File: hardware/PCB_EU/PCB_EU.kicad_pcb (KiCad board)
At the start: 4 copper layers, 100 x 100 mm, 200 parts, among them J101 24 V IN, J201 UART 3V3, J301 MEM2061 SPI, J401 SHT4x XH2.54-4P-90, J403 FLOAT / GND, J411 FAN1 2510-4P, J421 FAN2 2510-4P, J501 LED1 + / GND, J601 LED2 + / GND, J602 BAR2 + / GND, J701 PTC + / RETURN, J702 PUMP + / RETURN, Q102 IRF1010ESPBF, Q411 FAN1 AO3422, Q421 FAN2 AO3422, Q501 TK22E10N1, Q601 TK22E10N1, Q701 BC847B-DIO, Q702 BC857B, Q703 IRF1010ESPBF, Q704 AO3422, SW201 RESET, SW202 BOOT, U101 L7987 3A, U102 INA226, U201 AP63203WU-7, U202 ESP32-WROOM-32E-N4, U301 MCP7940N-I/SN, U401 USBLC6-2SC6, U402 USBLC6-2SC6, U501 LM3429MH/NOPB, U601 LM3429MH/NOPB, U802 LM2903D-ST, Y301 32.768k CL7p

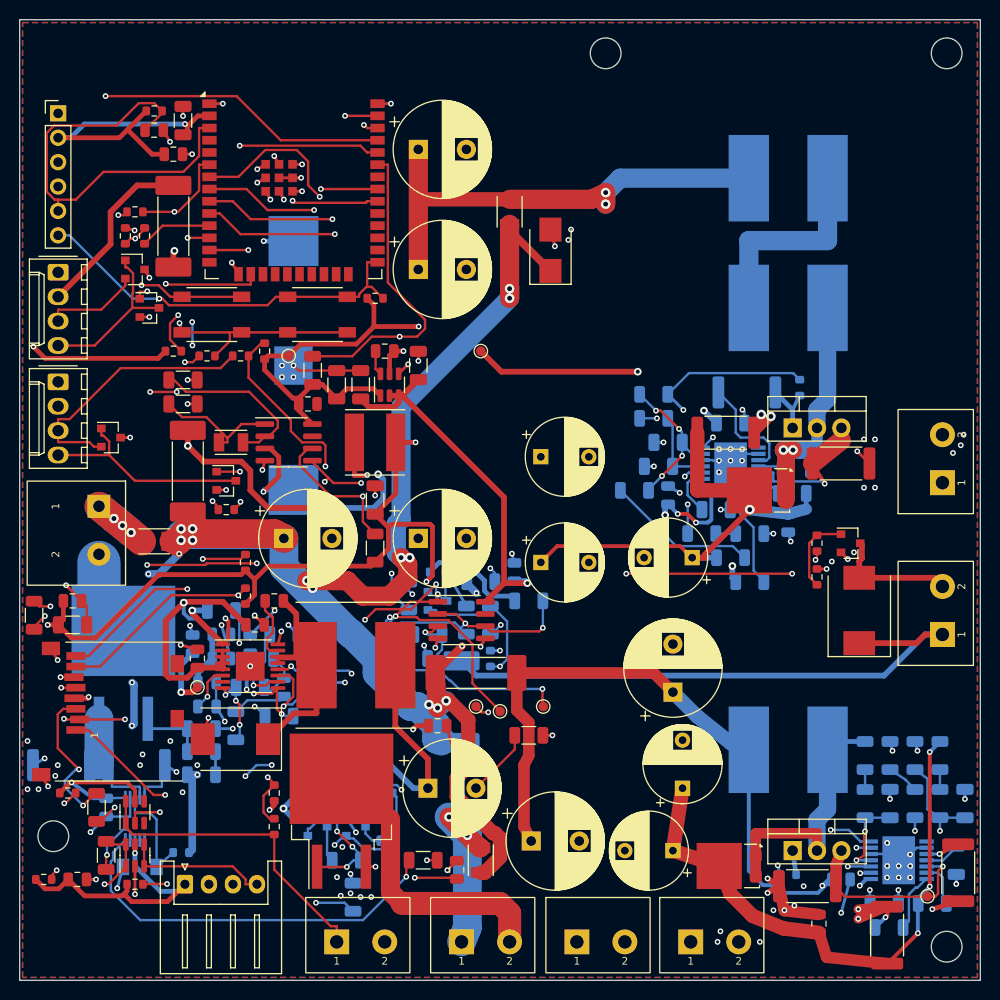
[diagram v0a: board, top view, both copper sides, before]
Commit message: PCB_EU: add polarity and component silkscreen
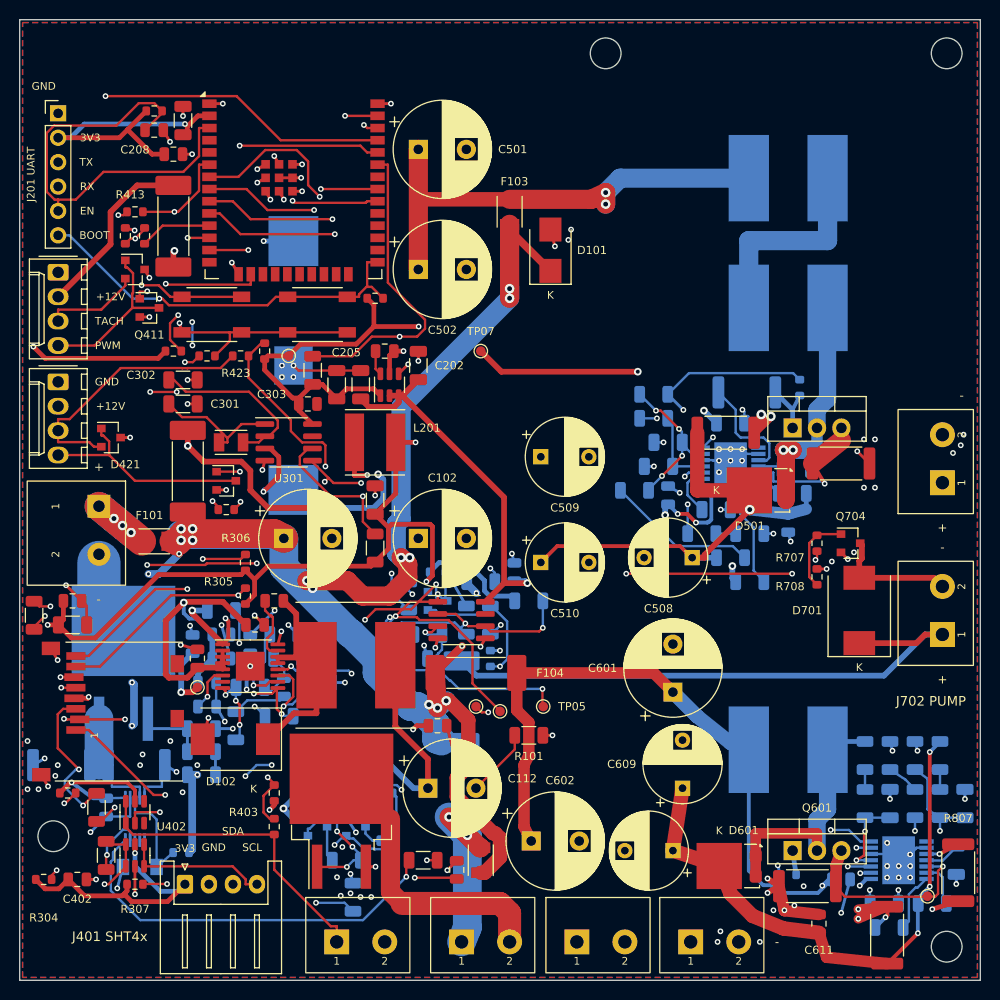
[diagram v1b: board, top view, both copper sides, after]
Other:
- board text added: "+"
- board text added: "+12V"
- board text added: "-"
- board text added: "3V3"
- board text added: "BOOT"
- board text added: "BT301"
- board text added: "BT301 CR2032"
- board text added: "C102"
- board text added: "C112"
- board text added: "C202"
- board text added: "C205"
- board text added: "C208"
- board text added: "C301"
- board text added: "C302"
- board text added: "C303"
- board text added: "C402"
- board text added: "C501"
- board text added: "C502"
- board text added: "C503"
- board text added: "C504"
- board text added: "C506"
- board text added: "C508"
- board text added: "C509"
- board text added: "C510"
- board text added: "C511"
- board text added: "C601"
- board text added: "C602"
- board text added: "C603"
- board text added: "C609"
- board text added: "C611"
- board text added: "C803"
- board text added: "D101"
- board text added: "D102"
- board text added: "D103"
- board text added: "D421"
- board text added: "D501"
- board text added: "D601"
- board text added: "D701"
- board text added: "EN"
- board text added: "F101"
- board text added: "F103"
- board text added: "F104"
- board text added: "F106"
- board text added: "GND"
- board text added: "J101 24V IN"
- board text added: "J201 UART"
- board text added: "J301 microSD"
- board text added: "J401 SHT4x"
- board text added: "J411 FAN1"
- board text added: "J421 FAN2"
- board text added: "J501 LED1"
- board text added: "J601 LED2"
- board text added: "J602 LED2 BAR2"
- board text added: "J701 PTC"
- board text added: "J702 PUMP"
- board text added: "K"
- board text added: "L201"
- board text added: "L501"
- board text added: "L502"
- board text added: "L601"
- board text added: "PWM"
- board text added: "Q102"
- board text added: "Q411"
- board text added: "Q601"
- board text added: "Q702"
- board text added: "Q704"
- board text added: "R101"
- board text added: "R102"
- board text added: "R103"
- board text added: "R104"
- board text added: "R105"
- board text added: "R106"
- board text added: "R107"
- board text added: "R108"
- board text added: "R113"
- board text added: "R304"
- board text added: "R305"
- board text added: "R306"
- board text added: "R307"
- board text added: "R403"
- board text added: "R413"
- board text added: "R423"
- board text added: "R503"
- board text added: "R504"
- board text added: "R508"
- board text added: "R509"
- board text added: "R510"
- board text added: "R511"
- board text added: "R604"
- board text added: "R606"
- board text added: "R609"
- board text added: "R611"
- board text added: "R701"
- board text added: "R702"
- board text added: "R703"
- board text added: "R704"
- board text added: "R705"
- board text added: "R706"
- board text added: "R707"
- board text added: "R708"
- board text added: "R804"
- board text added: "R807"
- board text added: "R808"
- board text added: "R810"
- board text added: "R811"
- board text added: "R813"
- board text added: "R817"
- board text added: "RX"
- board text added: "SCL"
- board text added: "SDA"
- board text added: "SIG"
- board text added: "TACH"
- board text added: "TP05"
- board text added: "TP06"
- board text added: "TP07"
- board text added: "TX"
- board text added: "U301"
- board text added: "U402"

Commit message: PCB_EU: reinforce supply copper and record selected stack
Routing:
- net +12V: track 197.8 -> 259.4 mm, vias 7 -> 11
- net GND: vias 138 -> 142
- net +24V_RAW: vias 3 -> 6
- net +24V_PTC: vias 3 -> 5
- net +24V_FUSED: vias 20 -> 22
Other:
- board text removed: "Q102"
- board text removed: "R305"
